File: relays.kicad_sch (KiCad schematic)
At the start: 0 parts

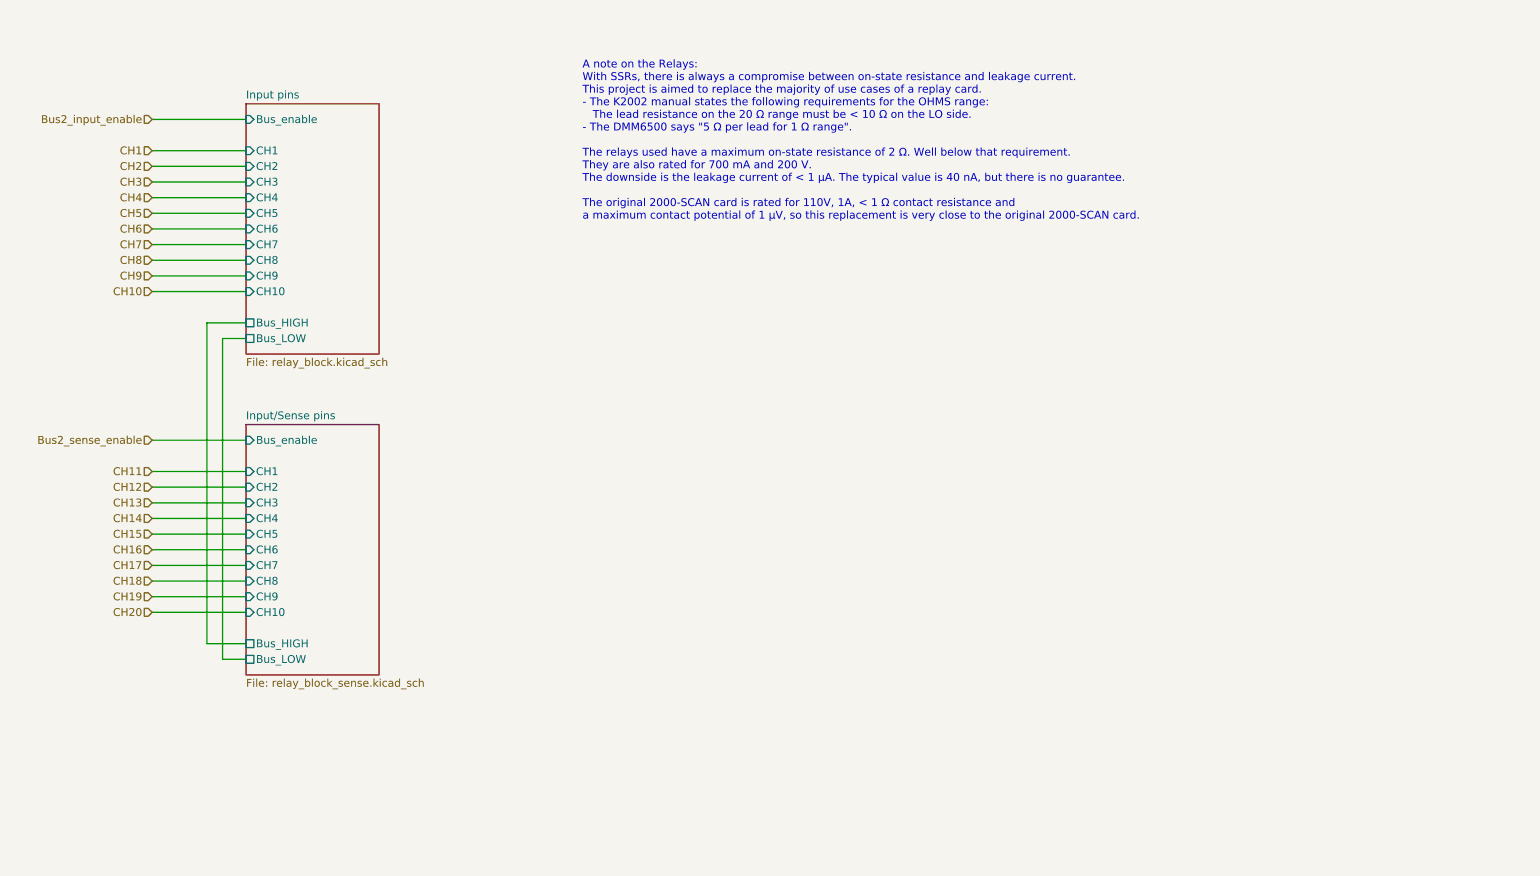
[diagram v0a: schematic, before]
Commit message: Replaced the STM32 microcontroller with an iCE40 FPGA
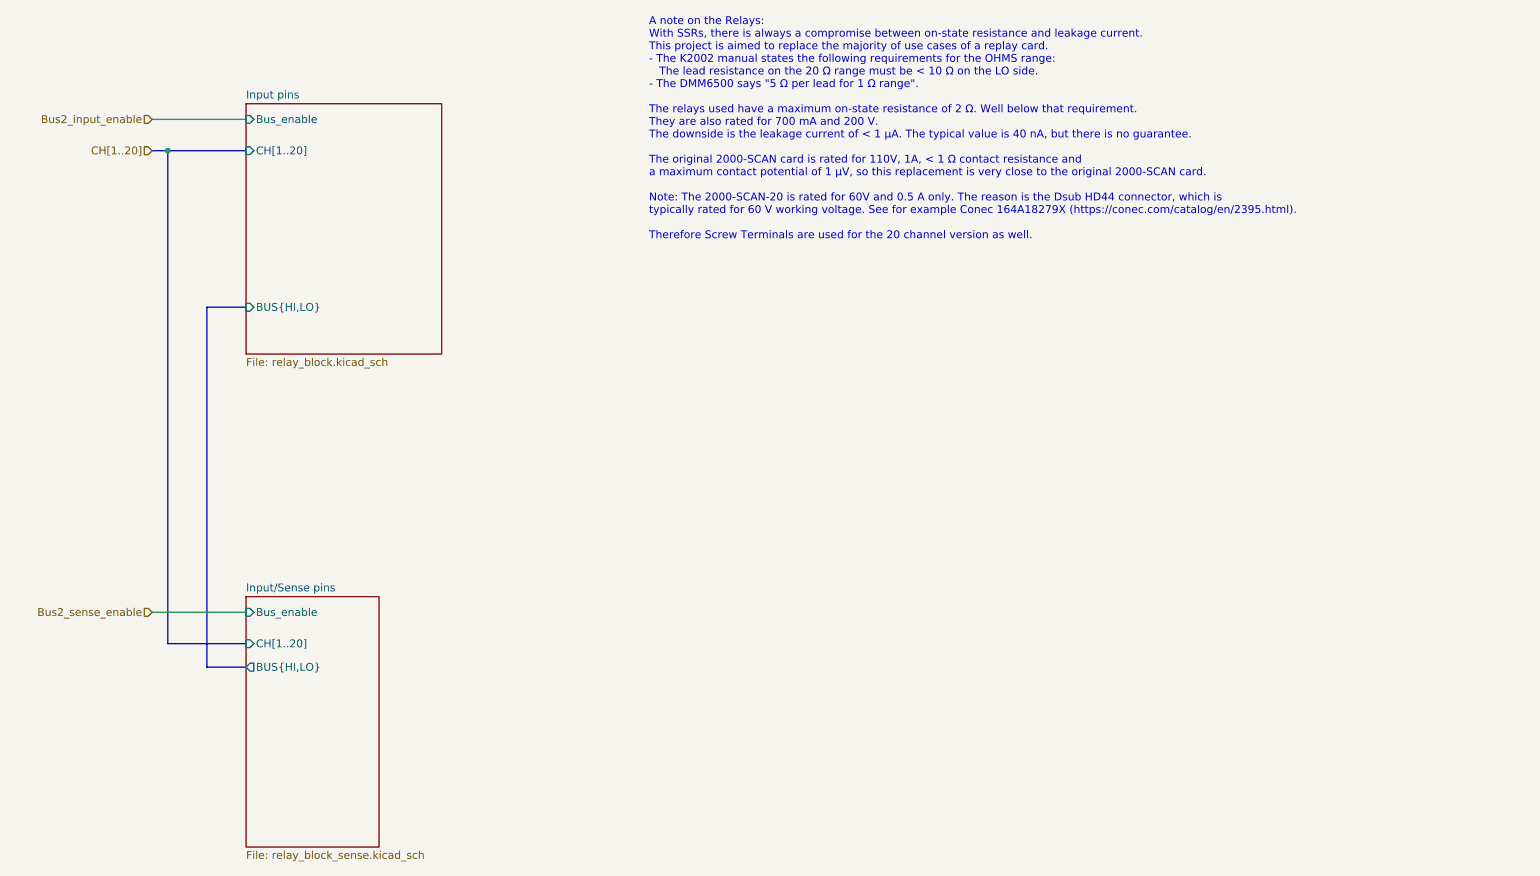
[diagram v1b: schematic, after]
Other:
- sheet Input pins ports: added BUS{HI,LO}, CH[1..20]; removed Bus_HIGH, Bus_LOW, CH1, CH10, CH2, CH3, CH4, CH5, CH6, CH7, CH8, CH9
- sheet Input/Sense pins ports: added BUS{HI,LO}, CH[1..20]; removed Bus_HIGH, Bus_LOW, CH1, CH10, CH2, CH3, CH4, CH5, CH6, CH7, CH8, CH9
